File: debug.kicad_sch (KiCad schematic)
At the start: 59 parts, among them J701 USB4105-GF-A, J702 2x10 pin IDC, U701 FT231XQ-R, U702 TCA9554PW

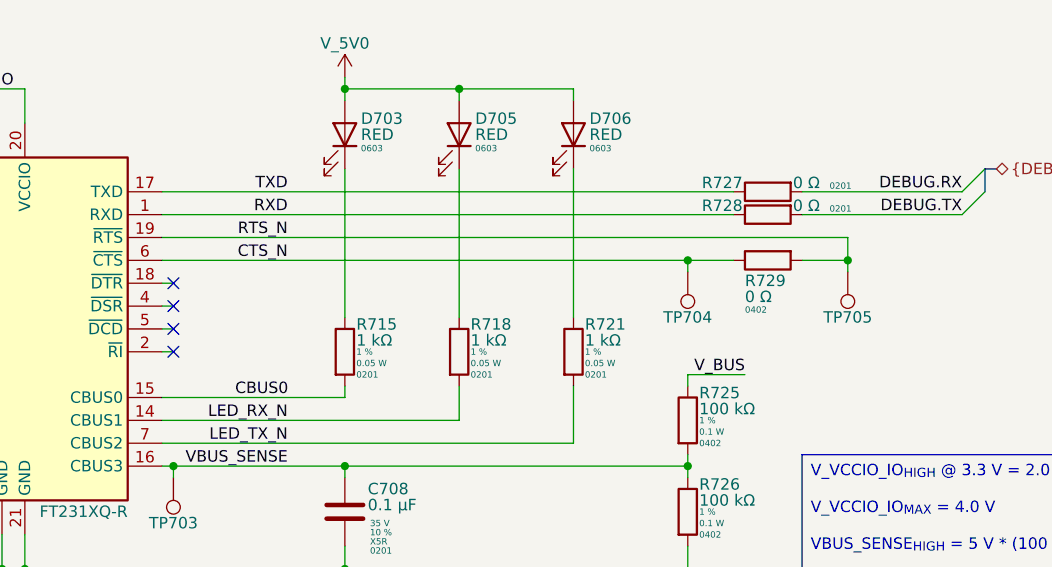
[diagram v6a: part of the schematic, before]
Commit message: Update 0402 footprints
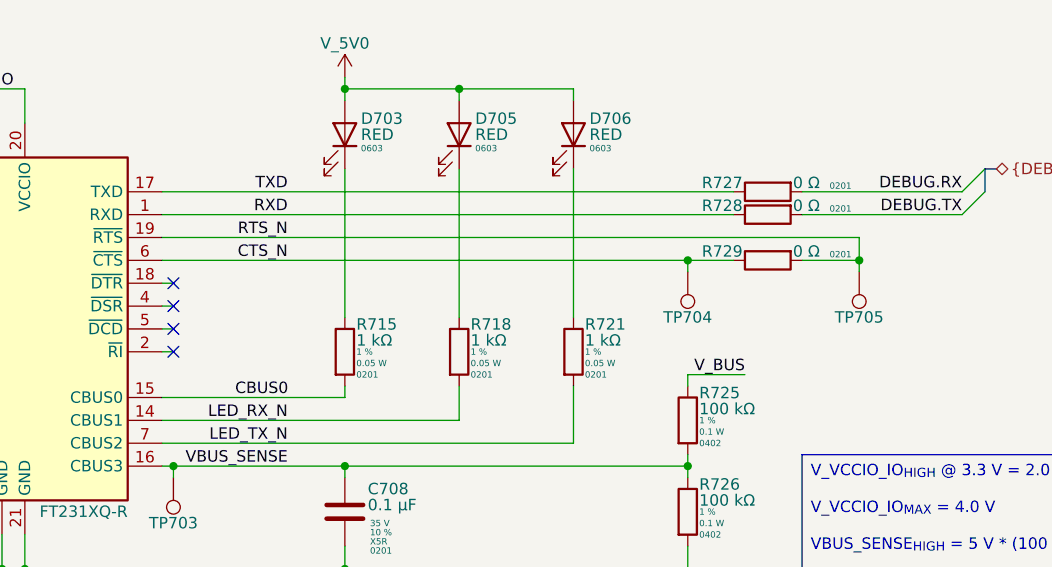
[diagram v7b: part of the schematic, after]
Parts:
- R725, R726: footprint perfect_footprints:R_0402_1005Metric -> perfect_footprints:R_0402_1005Metric_HDI
- R729: Size 0402 -> 0201
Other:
- moved on the sheet: TP705
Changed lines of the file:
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@@
 	)
 	(junction
-		(at 328.93 207.01)
-		(diameter 0)
-		(color 0 0 0 0)
-	)
-	(junction
 		(at 21.59 231.14)
 		(diameter 0)
@@
 		(color 0 0 0 0)
 	)
+	(junction
+		(at 330.2 207.01)
+		(diameter 0)
+		(color 0 0 0 0)
+	)
 	(no_connect
 		(at 147.32 227.33)
@@
 	(wire
 		(pts
-			(xy 323.85 207.01) (xy 328.93 207.01)
+			(xy 323.85 207.01) (xy 330.2 207.01)
 		)
 		(stroke
@@
 	(wire
 		(pts
-			(xy 328.93 208.28) (xy 328.93 207.01)
+			(xy 330.2 208.28) (xy 330.2 207.01)
 		)
 		(stroke
@@
 	(wire
 		(pts
-			(xy 328.93 207.01) (xy 328.93 204.47)
+			(xy 330.2 207.01) (xy 330.2 204.47)
 		)
 		(stroke
@@
 	(wire
 		(pts
-			(xy 252.73 204.47) (xy 328.93 204.47)
+			(xy 252.73 204.47) (xy 330.2 204.47)
 		)
 		(stroke
@@
 			)
 		)
-		(property "Footprint" "perfect_footprints:R_0402_1005Metric"
+		(property "Footprint" "perfect_footprints:R_0402_1005Metric_HDI"
 			(at 309.372 234.95 90)
 			(effects
@@
 	)
 	(symbol
-		(lib_name "R_3")
-		(lib_id "Device:R")
-		(at 320.04 207.01 90)
-		(mirror x)
-		(unit 1)
-		(exclude_from_sim no)
-		(in_bom yes)
-		(on_board yes)
-		(dnp no)
-		(property "Reference" "R729"
-			(at 317.5 208.534 90)
-			(effects
-				(font
-					(size 1.27 1.27)
-				)
-				(justify right top)
-			)
-		)
-		(property "Value" "0 Ω"
-			(at 317.5 210.312 90)
-			(effects
-				(font
-					(size 1.27 1.27)
-				)
-				(justify right top)
-			)
-		)
-		(property "Footprint" "perfect_footprints:R_0201_0603Metric"
-			(at 320.04 205.232 90)
-			(effects
-				(font
-					(size 1.27 1.27)
-				)
-				(hide yes)
-			)
-		)
-		(property "Datasheet" "https://industrial.panasonic.com/ww/products/pt/general-purpose-chip-resistors/models/ERJ1GN0R00C"
-			(at 320.04 207.01 0)
-			(effects
-				(font
-					(size 1.27 1.27)
-				)
-				(hide yes)
-			)
-		)
-		(property "Description" "0 Ohms Jumper Chip Resistor 0201 (0603 Metric) Thick Film"
-			(at 320.04 207.01 0)
-			(effects
-				(font
-					(size 1.27 1.27)
-				)
-				(hide yes)
-			)
-		)
-		(property "MPN" "ERJ-1GN0R00C"
-			(at 320.04 207.01 0)
-			(effects
-				(font
-					(size 1.27 1.27)
-				)
-				(hide yes)
-			)
-		)
-		(property "Manufacturer" "Panasonic Electronic Components"
-			(at 320.04 207.01 0)
-			(effects
-				(font
-					(size 1.27 1.27)
-				)
-				(hide yes)
-			)
-		)
-		(property "Size" "0402"
-			(at 317.5 212.09 90)
-			(effects
-				(font
-					(size 0.7 0.7)
-				)
-				(justify right top)
-			)
-		)
-		(property "Digi-Key Part Number" "P15979CT-ND"
-			(at 320.04 207.01 90)
-			(effects
-				(font
-					(size 1.27 1.27)
-				)
-				(hide yes)
-			)
-		)
-		(pin "2"
-		)
-		(pin "1"
-		)
-		(instances
-			(project "linux-sbc"
-				(path "/fa11a02f-8043-4153-ab69-88d766503017/5e32b227-0684-45b9-8c92-9550e4036164"
-					(reference "R729")
-					(unit 1)
-				)
-			)
-		)
-	)
-	(symbol
 		(lib_id "Device:C")
 		(at 203.2 234.95 0)
@@
 			)
 		)
-		(property "Footprint" "perfect_footprints:R_0402_1005Metric"
+		(property "Footprint" "perfect_footprints:R_0402_1005Metric_HDI"
 			(at 309.372 224.79 90)
 			(effects
@@
 	(symbol
 		(lib_id "Connector:TestPoint")
-		(at 328.93 208.28 180)
+		(at 330.2 208.28 180)
 		(unit 1)
 		(exclude_from_sim no)
@@
 		(dnp no)
 		(property "Reference" "TP705"
-			(at 328.93 212.598 0)
+			(at 330.2 212.598 0)
 			(effects
 				(font
@@
 		)
 		(property "Value" "TestPoint"
-			(at 326.39 211.582 90)
+			(at 327.66 211.582 90)
 			(effects
 				(font
@@
 		)
 		(property "Footprint" "TestPoint:TestPoint_Pad_D1.0mm"
-			(at 323.85 208.28 0)
+			(at 325.12 208.28 0)
 			(effects
 				(font
@@
 		)
 		(property "Datasheet" "~"
-			(at 323.85 208.28 0)
+			(at 325.12 208.28 0)
 			(effects
 				(font
@@
 		)
 		(property "Description" "test point"
-			(at 328.93 208.28 0)
+			(at 330.2 208.28 0)
 			(effects
 				(font
@@
 					(unit 1)
 				)
+			)
+		)
+	)
+	(symbol
+		(lib_name "R_2")
+		(lib_id "Device:R")
+		(at 320.04 207.01 90)
+		(mirror x)
+		(unit 1)
+		(exclude_from_sim no)
+		(in_bom yes)
+		(on_board yes)
+		(dnp no)
+		(property "Reference" "R729"
+			(at 317.246 206.756 90)
+			(effects
+				(font
+					(size 1.27 1.27)
+				)
+				(justify left bottom)
+			)
+		)
+		(property "Value" "0 Ω"
+			(at 322.834 206.756 90)
+			(effects
+				(font
+					(size 1.27 1.27)
+				)
+				(justify right bottom)
+			)
+		)
+		(property "Footprint" "perfect_footprints:R_0201_0603Metric"
+			(at 320.04 205.232 90)
+			(effects
+				(font
+					(size 1.27 1.27)
+				)
+				(hide yes)
+			)
+		)
+		(property "Datasheet" "https://industrial.panasonic.com/ww/products/pt/general-purpose-chip-resistors/models/ERJ1GN0R00C"
+			(at 320.04 207.01 0)
+			(effects
+				(font
+					(size 1.27 1.27)
+				)
+				(hide yes)
+			)
+		)
+		(property "Description" "0 Ohms Jumper Chip Resistor 0201 (0603 Metric) Thick Film"
+			(at 320.04 207.01 0)
+			(effects
+				(font
+					(size 1.27 1.27)
+				)
+				(hide yes)
+			)
+		)
+		(property "MPN" "ERJ-1GN0R00C"
+			(at 320.04 207.01 0)
+			(effects
+				(font
+					(size 1.27 1.27)
+				)
+				(hide yes)
+			)
+		)
+		(property "Manufacturer" "Panasonic Electronic Components"
+			(at 320.04 207.01 0)
+			(effects
+				(font
+					(size 1.27 1.27)
+				)
+				(hide yes)
+			)
+		)
+		(property "Size" "0201"
+			(at 326.898 206.756 90)
+			(effects
+				(font
+					(size 0.7 0.7)
+				)
+				(justify right bottom)
+			)
+		)
+		(property "Digi-Key Part Number" "P15979CT-ND"
+			(at 320.04 207.01 90)
+			(effects
+				(font
+					(size 1.27 1.27)
+				)
+				(hide yes)
+			)
+		)
+		(pin "2"
+		)
+		(pin "1"
+		)
+		(instances
+			(project "linux-sbc"
+				(path "/fa11a02f-8043-4153-ab69-88d766503017/5e32b227-0684-45b9-8c92-9550e4036164"
+					(reference "R729")
+					(unit 1)
+				)

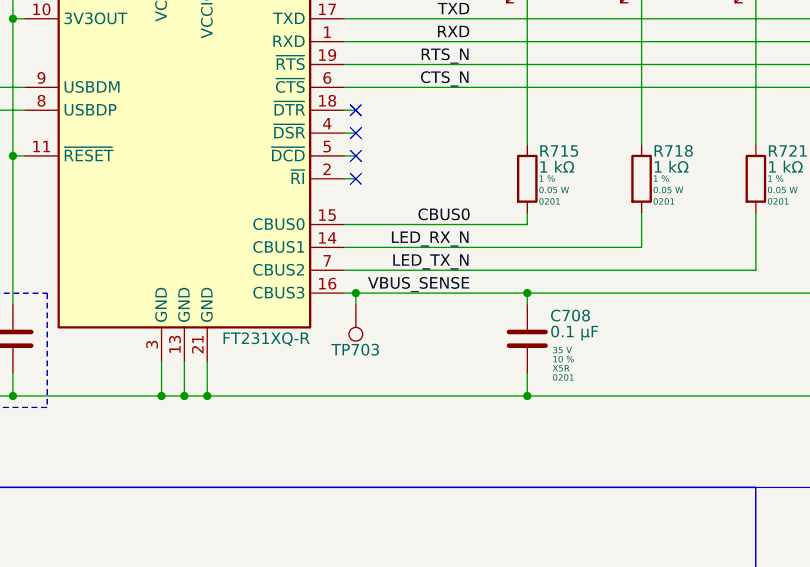
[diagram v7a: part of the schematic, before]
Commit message: Remove redundant test points and add bottom silkscreen
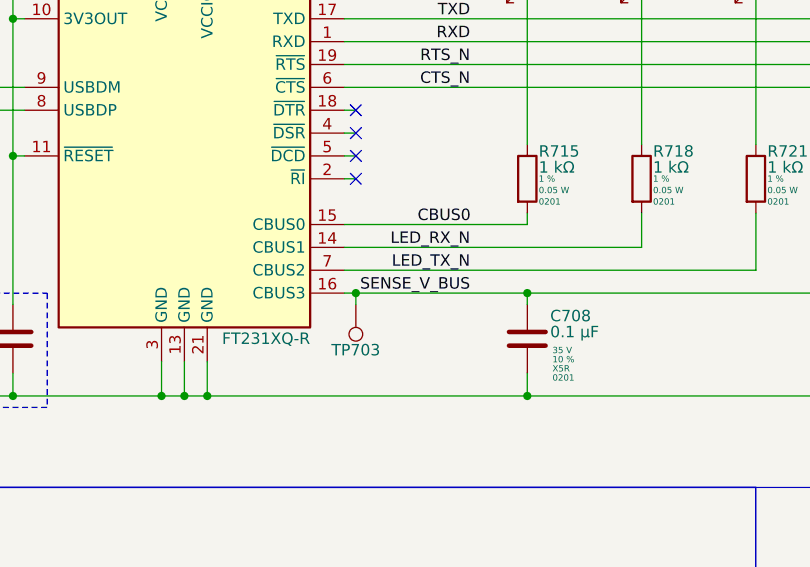
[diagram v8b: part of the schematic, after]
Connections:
- net VBUS_SENSE renamed SENSE_V_BUS
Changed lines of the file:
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@@
 		)
 	)
-	(label "VBUS_SENSE"
+	(label "SENSE_V_BUS"
 		(at 266.7 229.87 180)
 		(effects
